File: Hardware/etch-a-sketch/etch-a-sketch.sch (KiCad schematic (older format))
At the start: 37 parts, among them J1 USART, J2 Conn_02x05_Odd_Even, J3 OLED, J4 Power Connector, SW1 Encoder 1, SW2 Encoder 2, U1 AMS1117-3.3, U2 STM32F401RET6

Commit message: feat: assign all footprints
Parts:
- FB1, FB2: footprint (none) -> Inductor_SMD:L_0805_2012Metric
- H1, H2, H3, H4: footprint (none) -> MountingHole:MountingHole_4.3mm_M4_Pad_Via
- HSE1: footprint (none) -> Crystal:Crystal_SMD_3225-4Pin_3.2x2.5mm
- J1: footprint (none) -> Connector_PinSocket_2.54mm:PinSocket_1x02_P2.54mm_Vertical
- J2: footprint (none) -> Connector_PinHeader_1.27mm:PinHeader_2x05_P1.27mm_Vertical_SMD
- J3: footprint (none) -> Connector_PinHeader_2.54mm:PinHeader_1x05_P2.54mm_Vertical
- J4: footprint (none) -> Connector_USB:USB_Micro-B_Wuerth_629105150521
- R1, R5: footprint (none) -> Resistor_SMD:R_0603_1608Metric
- R2, R3, R4: footprint (none) -> Resistor_SMD:R_0402_1005Metric
- SW1, SW2: footprint (none) -> Rotary_Encoder:RotaryEncoder_Alps_EC11E-Switch_Vertical_H20mm
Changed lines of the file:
@@
 F 0 "SW1" H 6150 3900 50  0000 R CNN
 F 1 "Encoder 1" H 6250 3400 50  0000 R CNN
-F 2 "" H 5950 3810 50  0001 C CNN
+F 2 "Rotary_Encoder:RotaryEncoder_Alps_EC11E-Switch_Vertical_H20mm" H 5950 3810 50  0001 C CNN
 F 3 "~" H 6100 3910 50  0001 C CNN
 	1    6100 3650
@@
 F 0 "SW2" H 6150 4600 50  0000 R CNN
 F 1 "Encoder 2" H 6300 4100 50  0000 R CNN
-F 2 "" H 5950 4510 50  0001 C CNN
+F 2 "Rotary_Encoder:RotaryEncoder_Alps_EC11E-Switch_Vertical_H20mm" H 5950 4510 50  0001 C CNN
 F 3 "~" H 6100 4610 50  0001 C CNN
 	1    6100 4350
@@
 F 0 "FB1" V 1563 1100 50  0000 C CNN
 F 1 "100 @ 100MHz" V 1654 1100 50  0000 C CNN
-F 2 "" V 1730 1100 50  0001 C CNN
+F 2 "Inductor_SMD:L_0805_2012Metric" V 1730 1100 50  0001 C CNN
 F 3 "~" H 1800 1100 50  0001 C CNN
 	1    1800 1100
@@
 F 0 "FB2" V 3313 2650 50  0000 C CNN
 F 1 "100 @ 100MHz" V 3404 2650 50  0000 C CNN
-F 2 "" V 3480 2650 50  0001 C CNN
+F 2 "Inductor_SMD:L_0805_2012Metric" V 3480 2650 50  0001 C CNN
 F 3 "~" H 3550 2650 50  0001 C CNN
 	1    3550 2650
@@
 F 0 "HSE1" H 3650 6200 50  0000 L CNN
 F 1 "16MHz" H 3650 6100 50  0000 L CNN
-F 2 "" H 4000 6000 50  0001 C CNN
+F 2 "Crystal:Crystal_SMD_3225-4Pin_3.2x2.5mm" H 4000 6000 50  0001 C CNN
 F 3 "~" H 4000 6000 50  0001 C CNN
 	1    4000 6000
@@
 F 0 "R4" V 4254 6000 50  0000 C CNN
 F 1 "220" V 4345 6000 50  0000 C CNN
-F 2 "" H 4450 6000 50  0001 C CNN
+F 2 "Resistor_SMD:R_0402_1005Metric" H 4450 6000 50  0001 C CNN
 F 3 "~" H 4450 6000 50  0001 C CNN
 	1    4450 6000
@@
 F 0 "R2" H 3909 3696 50  0000 L CNN
 F 1 "10k" H 3909 3605 50  0000 L CNN
-F 2 "" H 3850 3650 50  0001 C CNN
+F 2 "Resistor_SMD:R_0402_1005Metric" H 3850 3650 50  0001 C CNN
 F 3 "~" H 3850 3650 50  0001 C CNN
 	1    3850 3650
@@
 F 0 "R3" H 4259 3696 50  0000 L CNN
 F 1 "10k" H 4259 3605 50  0000 L CNN
-F 2 "" H 4200 3650 50  0001 C CNN
+F 2 "Resistor_SMD:R_0402_1005Metric" H 4200 3650 50  0001 C CNN
 F 3 "~" H 4200 3650 50  0001 C CNN
 	1    4200 3650
@@
 F 0 "J2" H 6000 3167 50  0000 C CNN
 F 1 "Conn_02x05_Odd_Even" H 6000 3076 50  0000 C CNN
-F 2 "" H 5950 2750 50  0001 C CNN
+F 2 "Connector_PinHeader_1.27mm:PinHeader_2x05_P1.27mm_Vertical_SMD" H 5950 2750 50  0001 C CNN
 F 3 "~" H 5950 2750 50  0001 C CNN
 	1    5950 2750
@@
 F 0 "R5" H 3259 6846 50  0000 L CNN
 F 1 "2k2" H 3259 6755 50  0000 L CNN
-F 2 "" H 3200 6800 50  0001 C CNN
+F 2 "Resistor_SMD:R_0603_1608Metric" H 3200 6800 50  0001 C CNN
 F 3 "~" H 3200 6800 50  0001 C CNN
 	1    3200 6800
@@
 F 0 "R1" H 3509 1396 50  0000 L CNN
 F 1 "2k2" H 3509 1305 50  0000 L CNN
-F 2 "" H 3450 1350 50  0001 C CNN
+F 2 "Resistor_SMD:R_0603_1608Metric" H 3450 1350 50  0001 C CNN
 F 3 "~" H 3450 1350 50  0001 C CNN
 	1    3450 1350
@@
 F 0 "J1" V 6714 2212 50  0000 R CNN
 F 1 "USART" V 6623 2212 50  0000 R CNN
-F 2 "" H 6750 2400 50  0001 C CNN
+F 2 "Connector_PinSocket_2.54mm:PinSocket_1x02_P2.54mm_Vertical" H 6750 2400 50  0001 C CNN
 F 3 "~" H 6750 2400 50  0001 C CNN
 	1    6750 2400
@@
 F 0 "J3" V 5622 5780 50  0000 L CNN
 F 1 "OLED" V 5713 5780 50  0000 L CNN
-F 2 "" H 5750 5500 50  0001 C CNN
+F 2 "Connector_PinHeader_2.54mm:PinHeader_1x05_P2.54mm_Vertical" H 5750 5500 50  0001 C CNN
 F 3 "~" H 5750 5500 50  0001 C CNN
 	1    5750 5500
@@
 F 0 "H2" V 7654 2750 50  0000 L CNN
 F 1 "MountingHole_Pad" V 7745 2750 50  0000 L CNN
-F 2 "" H 7700 2600 50  0001 C CNN
+F 2 "MountingHole:MountingHole_4.3mm_M4_Pad_Via" H 7700 2600 50  0001 C CNN
 F 3 "~" H 7700 2600 50  0001 C CNN
 	1    7700 2600
@@
 F 0 "H3" V 7654 3000 50  0000 L CNN
 F 1 "MountingHole_Pad" V 7745 3000 50  0000 L CNN
-F 2 "" H 7700 2850 50  0001 C CNN
+F 2 "MountingHole:MountingHole_4.3mm_M4_Pad_Via" H 7700 2850 50  0001 C CNN
 F 3 "~" H 7700 2850 50  0001 C CNN
 	1    7700 2850
@@
 F 0 "H4" V 7654 3250 50  0000 L CNN
 F 1 "MountingHole_Pad" V 7745 3250 50  0000 L CNN
-F 2 "" H 7700 3100 50  0001 C CNN
+F 2 "MountingHole:MountingHole_4.3mm_M4_Pad_Via" H 7700 3100 50  0001 C CNN
 F 3 "~" H 7700 3100 50  0001 C CNN
 	1    7700 3100
@@
 F 0 "H1" V 7654 2500 50  0000 L CNN
 F 1 "MountingHole_Pad" V 7745 2500 50  0000 L CNN
-F 2 "" H 7700 2350 50  0001 C CNN
+F 2 "MountingHole:MountingHole_4.3mm_M4_Pad_Via" H 7700 2350 50  0001 C CNN
 F 3 "~" H 7700 2350 50  0001 C CNN
 	1    7700 2350
@@
 F 0 "J4" H 5807 6817 50  0000 C CNN
 F 1 "Power Connector" H 5807 6726 50  0000 C CNN
-F 2 "" H 5900 6300 50  0001 C CNN
+F 2 "Connector_USB:USB_Micro-B_Wuerth_629105150521" H 5900 6300 50  0001 C CNN
 F 3 "~" H 5900 6300 50  0001 C CNN
 	1    5750 6350

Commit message: feat: associate correct footprint for OLED connector
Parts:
- J3: footprint Connector_PinHeader_2.54mm:PinHeader_1x05_P2.54mm_Vertical -> 1.12_mono_oled:THT
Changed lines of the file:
@@
 F 0 "J3" V 5622 5780 50  0000 L CNN
 F 1 "OLED" V 5713 5780 50  0000 L CNN
-F 2 "Connector_PinHeader_2.54mm:PinHeader_1x05_P2.54mm_Vertical" H 5750 5500 50  0001 C CNN
+F 2 "1.12_mono_oled:THT" H 5750 5500 50  0001 C CNN
 F 3 "~" H 5750 5500 50  0001 C CNN
 	1    5750 5500

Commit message: fix: actually maybe better to keep the OLED socketed
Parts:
- J3: footprint 1.12_mono_oled:THT -> Connector_PinSocket_2.54mm:PinSocket_1x05_P2.54mm_Vertical
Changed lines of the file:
@@
 F 0 "J3" V 5622 5780 50  0000 L CNN
 F 1 "OLED" V 5713 5780 50  0000 L CNN
-F 2 "1.12_mono_oled:THT" H 5750 5500 50  0001 C CNN
+F 2 "Connector_PinSocket_2.54mm:PinSocket_1x05_P2.54mm_Vertical" H 5750 5500 50  0001 C CNN
 F 3 "~" H 5750 5500 50  0001 C CNN
 	1    5750 5500

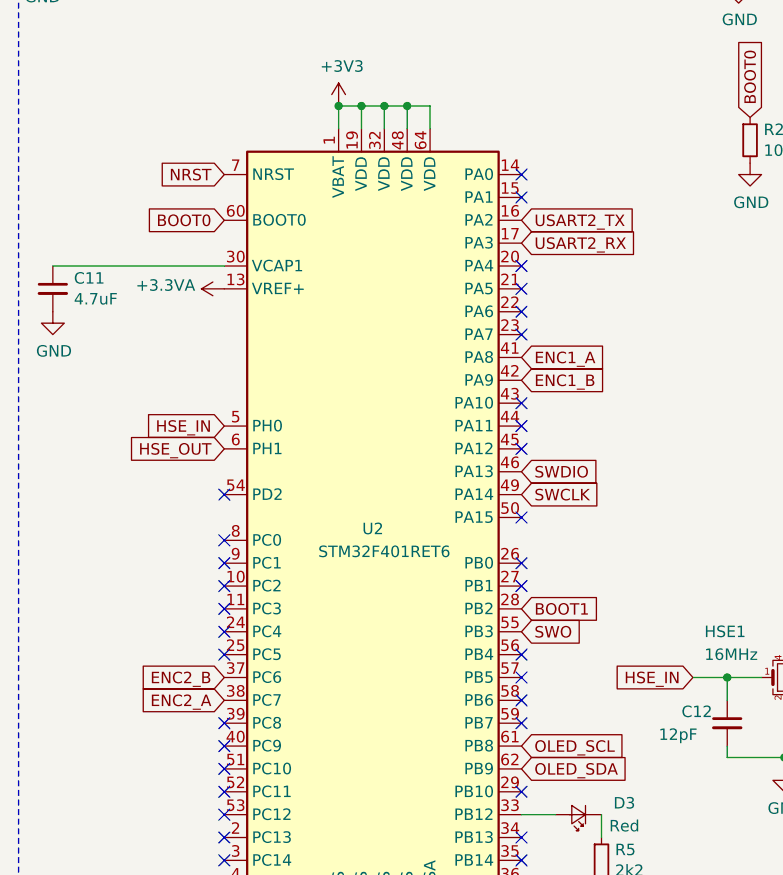
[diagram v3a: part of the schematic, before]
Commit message: refactor: reposition encoders
- Move ENC2 to use PA0 and PA2 so they don't need to cross to the other
  side of the MCU.
- Swap ENC1's A and B pins so they don't cross each other.
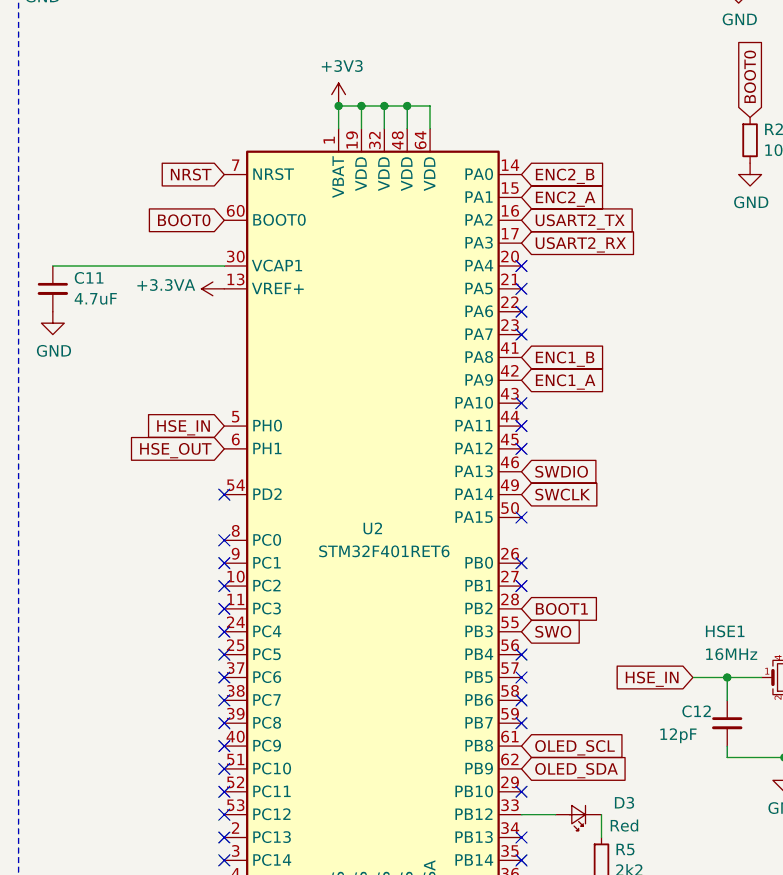
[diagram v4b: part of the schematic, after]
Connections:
- net ENC1_A: now also U2.42 (PA9); no longer U2.41 (PA8)
- net ENC1_B: now also U2.41 (PA8); no longer U2.42 (PA9)
- net ENC2_A: now also U2.15 (PA1); no longer U2.38 (PC7)
- net ENC2_B: now also U2.14 (PA0); no longer U2.37 (PC6)
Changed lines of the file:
@@
 NoConn ~ 2850 4300
 NoConn ~ 2850 4200
-NoConn ~ 2850 3900
-NoConn ~ 2850 3800
 NoConn ~ 6400 4450
 NoConn ~ 6400 4250
@@
 Text GLabel 2850 6300 2    50   Input ~ 0
 OLED_SCL
+Text GLabel 2850 4700 2    50   Input ~ 0
+ENC1_A
 Text GLabel 2850 4600 2    50   Input ~ 0
-ENC1_A
-Text GLabel 2850 4700 2    50   Input ~ 0
 ENC1_B
-Text GLabel 1550 6100 0    50   Input ~ 0
+Text GLabel 2850 3900 2    50   Input ~ 0
 ENC2_A
-Text GLabel 1550 6000 0    50   Input ~ 0
+Text GLabel 2850 3800 2    50   Input ~ 0
 ENC2_B
 Text GLabel 6250 2950 2    50   Input ~ 0
@@
 Wire Wire Line
 	6050 6150 6300 6150
+NoConn ~ 1550 6000
+NoConn ~ 1550 6100
 $EndSCHEMATC

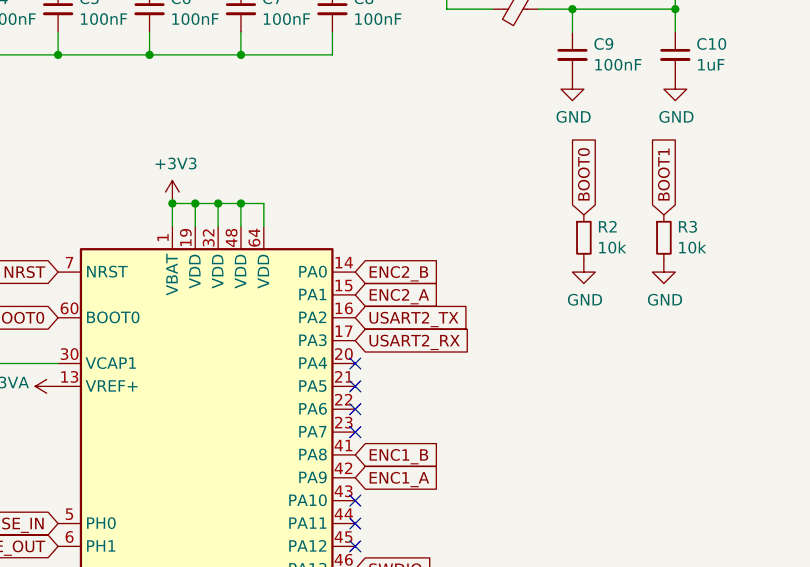
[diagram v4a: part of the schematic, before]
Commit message: feat: move USART to top, rearrange encoder 2 pins
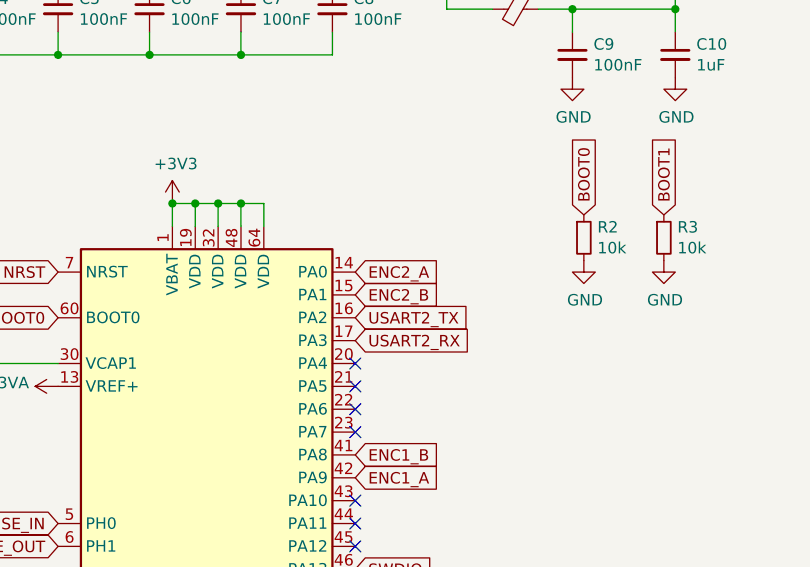
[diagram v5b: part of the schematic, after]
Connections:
- net ENC2_A: now also U2.14 (PA0); no longer U2.15 (PA1)
- net ENC2_B: now also U2.15 (PA1); no longer U2.14 (PA0)
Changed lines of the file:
@@
 Text GLabel 2850 4600 2    50   Input ~ 0
 ENC1_B
+Text GLabel 2850 3800 2    50   Input ~ 0
+ENC2_A
 Text GLabel 2850 3900 2    50   Input ~ 0
-ENC2_A
-Text GLabel 2850 3800 2    50   Input ~ 0
 ENC2_B
 Text GLabel 6250 2950 2    50   Input ~ 0

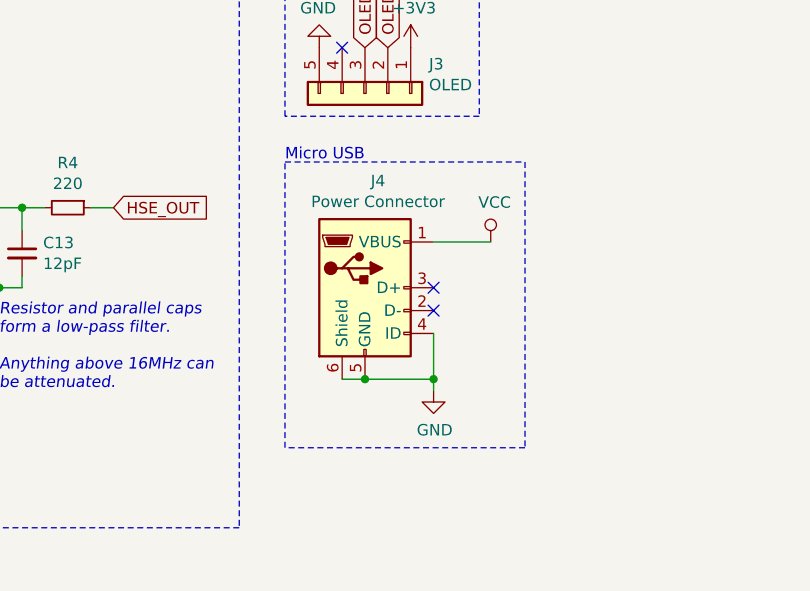
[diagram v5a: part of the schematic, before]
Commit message: feat: change micro USB footprint to 10118194
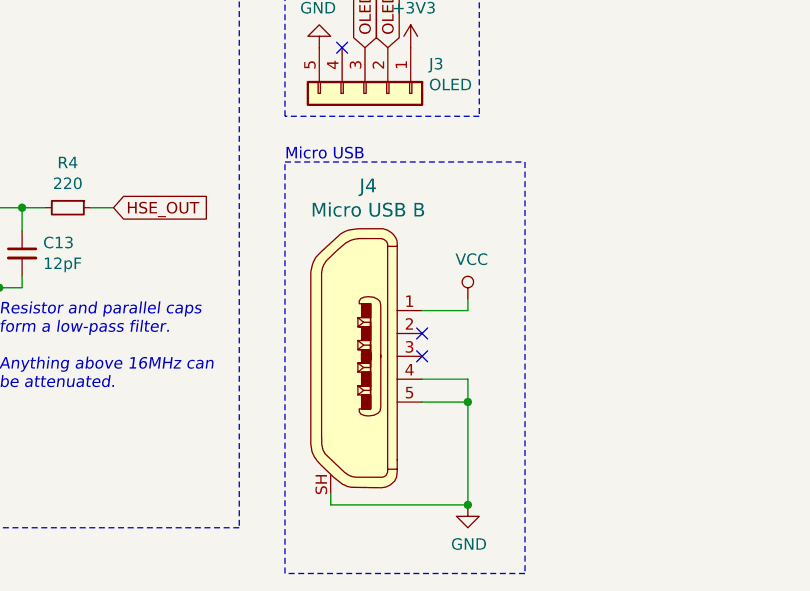
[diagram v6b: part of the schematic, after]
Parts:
- removed J4: Power Connector, Connector_USB:USB_Micro-B_Wuerth_629105150521, symbol Connector:USB_B_Mini
- added J4: Micro USB B, digikey-footprints:USB_Micro_B_Female_10118194-0001LF, symbol dk_USB-DVI-HDMI-Connectors:10118194-0001LF
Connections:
- net GND: now also J4.4, J4.5, J4.SH
- net VCC: now also J4.1
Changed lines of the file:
@@
 Text Notes 7450 2200 0    50   ~ 0
 Mounting Holes
+Wire Notes Line
+	5400 5800 6450 5800
+Wire Notes Line
+	6450 5800 6450 7600
+Wire Notes Line
+	6450 7600 5400 7600
+Wire Notes Line
+	5400 7600 5400 5800
+Text Notes 5400 5800 0    50   ~ 0
+Micro USB
+NoConn ~ 1550 6000
+NoConn ~ 1550 6100
 $Comp
-L Connector:USB_B_Mini J4
-U 1 1 5EDAFB76
-P 5750 6350
-F 0 "J4" H 5807 6817 50  0000 C CNN
-F 1 "Power Connector" H 5807 6726 50  0000 C CNN
-F 2 "Connector_USB:USB_Micro-B_Wuerth_629105150521" H 5900 6300 50  0001 C CNN
-F 3 "~" H 5900 6300 50  0001 C CNN
-	1    5750 6350
+L dk_USB-DVI-HDMI-Connectors:10118194-0001LF J4
+U 1 1 5EACED3E
+P 5700 6650
+F 0 "J4" H 5764 7395 60  0000 C CNN
+F 1 "Micro USB B" H 5764 7289 60  0000 C CNN
+F 2 "digikey-footprints:USB_Micro_B_Female_10118194-0001LF" H 5900 6850 60  0001 L CNN
+F 3 "http://www.amphenol-icc.com/media/wysiwyg/files/drawing/10118194.pdf" H 5900 6950 60  0001 L CNN
+F 4 "609-4618-1-ND" H 5900 7050 60  0001 L CNN "Digi-Key_PN"
+F 5 "10118194-0001LF" H 5900 7150 60  0001 L CNN "MPN"
+F 6 "Connectors, Interconnects" H 5900 7250 60  0001 L CNN "Category"
+F 7 "USB, DVI, HDMI Connectors" H 5900 7350 60  0001 L CNN "Family"
+F 8 "http://www.amphenol-icc.com/media/wysiwyg/files/drawing/10118194.pdf" H 5900 7450 60  0001 L CNN "DK_Datasheet_Link"
+F 9 "/product-detail/en/amphenol-icc-fci/10118194-0001LF/609-4618-1-ND/2785382" H 5900 7550 60  0001 L CNN "DK_Detail_Page"
+F 10 "CONN RCPT USB2.0 MICRO B SMD R/A" H 5900 7650 60  0001 L CNN "Description"
+F 11 "Amphenol ICC (FCI)" H 5900 7750 60  0001 L CNN "Manufacturer"
+F 12 "Active" H 5900 7850 60  0001 L CNN "Status"
+	1    5700 6650
 	1    0    0    -1
 $EndComp
-NoConn ~ 6050 6350
-NoConn ~ 6050 6450
+NoConn ~ 6000 6550
+NoConn ~ 6000 6650
+Wire Wire Line
+	6000 6450 6200 6450
+Wire Wire Line
+	6200 6450 6200 6400
 $Comp
 L power:GND #PWR025
-U 1 1 5EDBF07A
-P 6050 6800
-F 0 "#PWR025" H 6050 6550 50  0001 C CNN
-F 1 "GND" H 6055 6627 50  0000 C CNN
-F 2 "" H 6050 6800 50  0001 C CNN
-F 3 "" H 6050 6800 50  0001 C CNN
-	1    6050 6800
+U 1 1 5EAE82FD
+P 6200 7300
+F 0 "#PWR025" H 6200 7050 50  0001 C CNN
+F 1 "GND" H 6205 7127 50  0000 C CNN
+F 2 "" H 6200 7300 50  0001 C CNN
+F 3 "" H 6200 7300 50  0001 C CNN
+	1    6200 7300
 	1    0    0    -1
 $EndComp
 Wire Wire Line
-	5750 6750 6050 6750
+	6000 6750 6200 6750
 Wire Wire Line
-	6050 6750 6050 6800
+	6200 6750 6200 6850
 Wire Wire Line
-	6050 6550 6050 6750
-Connection ~ 6050 6750
+	6000 6850 6200 6850
+Connection ~ 6200 6850
 Wire Wire Line
-	5650 6750 5750 6750
-Connection ~ 5750 6750
-Wire Notes Line
-	5400 5800 6450 5800
-Wire Notes Line
-	6450 5800 6450 7050
-Wire Notes Line
-	6450 7050 5400 7050
-Wire Notes Line
-	5400 7050 5400 5800
-Text Notes 5400 5800 0    50   ~ 0
-Micro USB
+	6200 6850 6200 7300
+Wire Wire Line
+	5600 7250 5600 7300
+Wire Wire Line
+	5600 7300 6200 7300
+Connection ~ 6200 7300
 $Comp
-L power:VCC #PWR0102
-U 1 1 5EDE1CBE
-P 6300 6150
-F 0 "#PWR0102" H 6300 6000 50  0001 C CNN
-F 1 "VCC" H 6317 6323 50  0000 C CNN
-F 2 "" H 6300 6150 50  0001 C CNN
-F 3 "" H 6300 6150 50  0001 C CNN
-	1    6300 6150
+L power:VCC #PWR024
+U 1 1 5EAFBEE0
+P 6200 6400
+F 0 "#PWR024" H 6200 6250 50  0001 C CNN
+F 1 "VCC" H 6217 6573 50  0000 C CNN
+F 2 "" H 6200 6400 50  0001 C CNN
+F 3 "" H 6200 6400 50  0001 C CNN
+	1    6200 6400
 	1    0    0    -1
 $EndComp
-Wire Wire Line
-	6050 6150 6300 6150
-NoConn ~ 1550 6000
-NoConn ~ 1550 6100
 $EndSCHEMATC

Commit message: feat: change SWD connector to through-hole
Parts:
- J2: footprint Connector_PinHeader_1.27mm:PinHeader_2x05_P1.27mm_Vertical_SMD -> Connector_PinHeader_1.27mm:PinHeader_2x05_P1.27mm_Vertical
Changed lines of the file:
@@
 F 0 "J2" H 6000 3167 50  0000 C CNN
 F 1 "Conn_02x05_Odd_Even" H 6000 3076 50  0000 C CNN
-F 2 "Connector_PinHeader_1.27mm:PinHeader_2x05_P1.27mm_Vertical_SMD" H 5950 2750 50  0001 C CNN
+F 2 "Connector_PinHeader_1.27mm:PinHeader_2x05_P1.27mm_Vertical" H 5950 2750 50  0001 C CNN
 F 3 "~" H 5950 2750 50  0001 C CNN
 	1    5950 2750
